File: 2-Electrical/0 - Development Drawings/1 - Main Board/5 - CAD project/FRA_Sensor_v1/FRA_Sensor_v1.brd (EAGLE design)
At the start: 100 x 100 mm, 179 parts, among them IC1 CP2101, IC2 LMV611, IC3 TS520533, IC4 ADS1115BQDGSRQ1, IC5 ADS1115BQDGSRQ1, IC6 ADS1115BQDGSRQ1, J2 ETH_CONN, J5 WM9734TR-ND, J8 1140084168, Q1 Si2300DS, Q2 FDN306P, Q3 Si2300DS, Q4 Si2300DS, Q5 Si2300DS, Q6 Si2300DS, Q7 100A/100V/6.8mΩ, T1 BC847, T2 BC847, T3 BC847, U2 ESP-WROOM-32, X1 TB001-500-02BE, Y3 32.768kHz

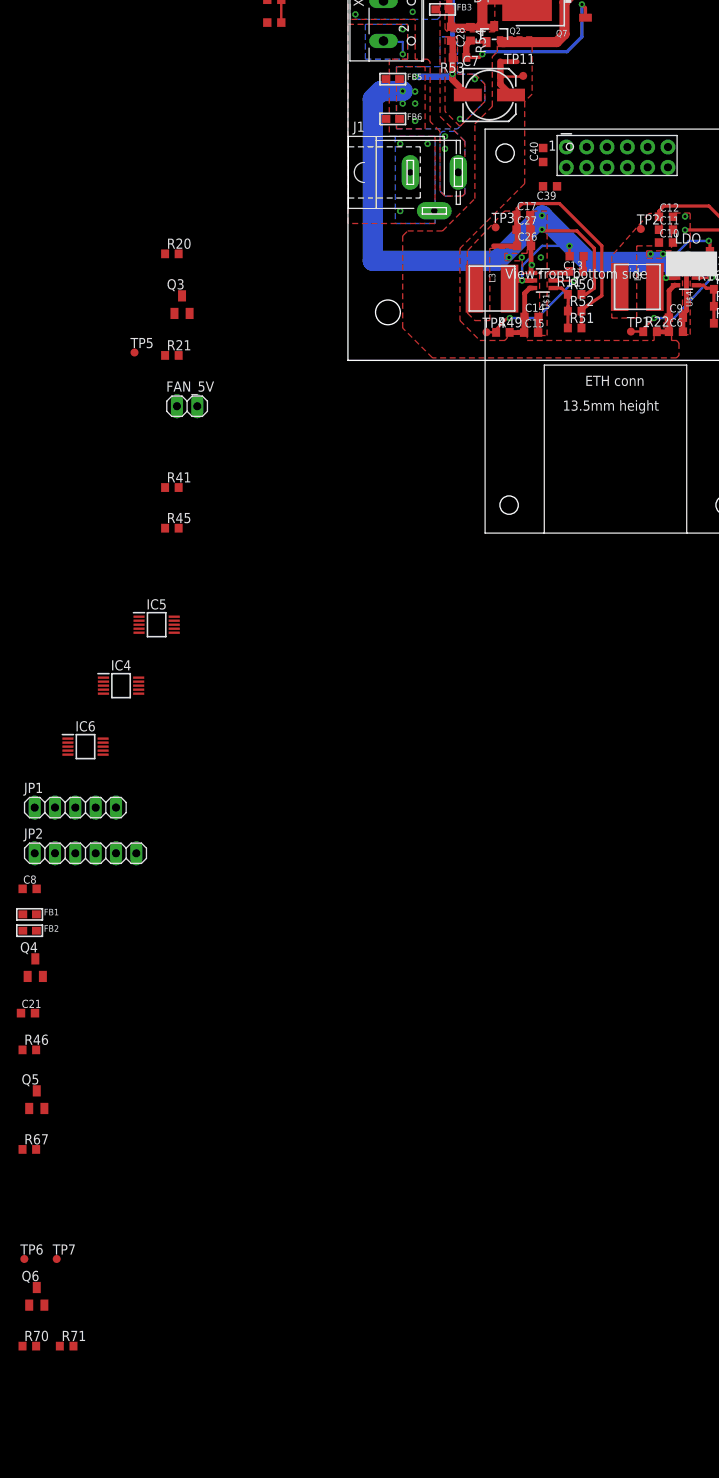
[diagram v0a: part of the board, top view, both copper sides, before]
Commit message: sch cap miltuplier add
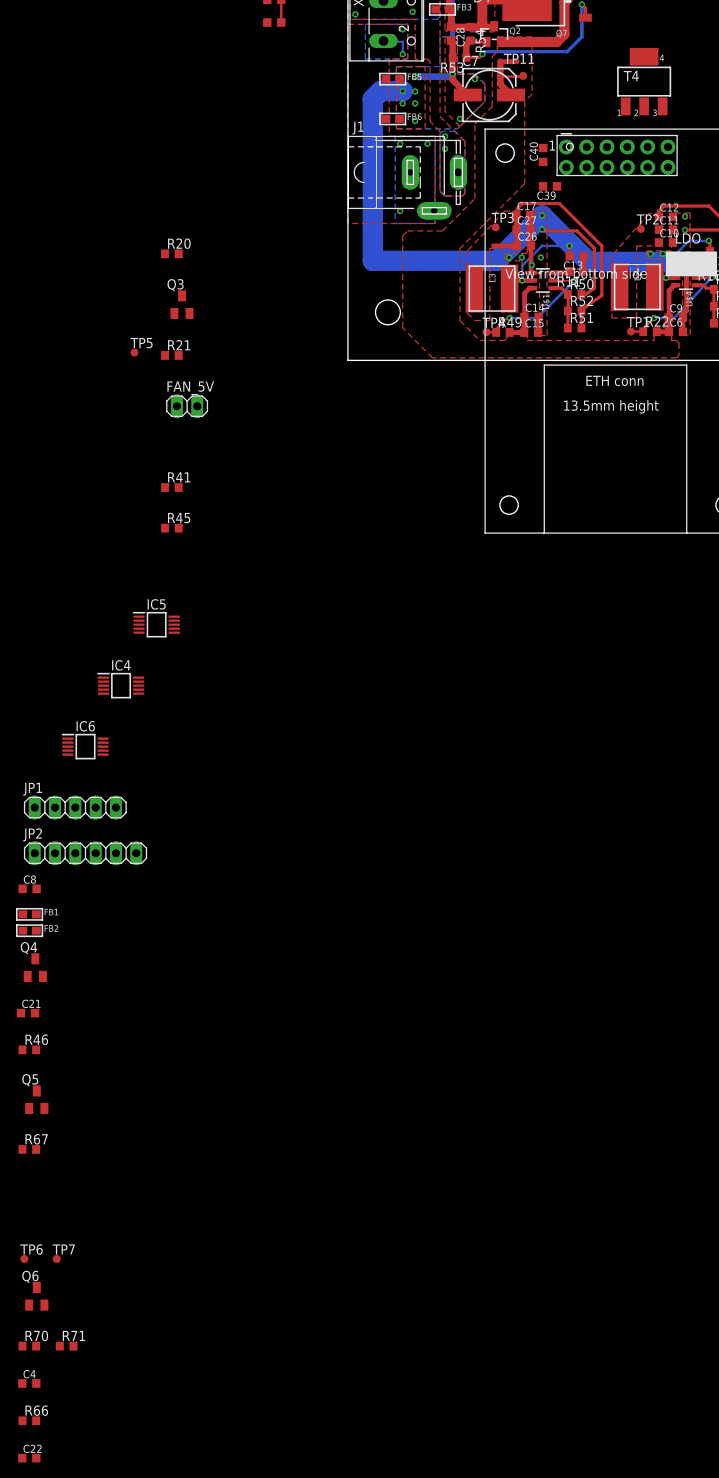
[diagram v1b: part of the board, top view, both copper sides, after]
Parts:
- added C22, C4: 10u, resistor:C0603K
- added R66: 10k, resistor:R0603
- added T4: (no value), transistor-neu-to92:SOT223
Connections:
- new net N$12: C22.1, C4.1, R66.2, T4.1
- new net VIN_FILT: T4.3
- net GND: now also C22.2, C4.2
- net VIN_PROTECTED: now also R66.1, T4.4
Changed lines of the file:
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@@
 <element name="FB6" library="microbuilder" package="0603" value="" x="5.6007" y="30.18155"/>
 <element name="Q7" library="microbuilder" package="TO252" value="100A/100V/6.8mΩ" x="24.892" y="45.11675" rot="R90"/>
+<element name="T4" library="transistor-neu-to92" package="SOT223" value="" x="37.02685" y="34.8488"/>
+<element name="C4" library="resistor" package="C0603K" value="10u" x="-39.8272" y="-127.88265"/>
+<element name="R66" library="resistor" package="R0603" value="10k" x="-39.8272" y="-132.5499"/>
+<element name="C22" library="resistor" package="C0603K" value="10u" x="-39.8272" y="-137.21715"/>
 </elements>
 <signals>
@@
 <wire x1="13.0683" y1="40.1206" x2="12.9032" y2="39.9555" width="0.6096" layer="16"/>
 <wire x1="14.99485" y1="49.02345" x2="16.89485" y2="49.02345" width="0.6096" layer="1"/>
-<wire x1="85.375" y1="56.06415" x2="87.9856" y2="65.99785" width="0" layer="19" extent="1-1"/>
-<wire x1="98.79" y1="41.34915" x2="96.76765" y2="49.1617" width="0" layer="19" extent="1-1"/>
-<wire x1="66.421" y1="17.907" x2="75.40625" y2="17.6276" width="0" layer="19" extent="1-1"/>
-<wire x1="65.408275" y1="12.8404125" x2="66.421" y2="17.907" width="0" layer="19" extent="1-1"/>
-<wire x1="58.801" y1="17.907" x2="66.421" y2="17.907" width="0" layer="19" extent="1-1"/>
-<wire x1="59.93" y1="22.86" x2="58.801" y2="17.907" width="0" layer="19" extent="1-1"/>
-<wire x1="50.927" y1="15.875" x2="58.801" y2="17.907" width="0" layer="19" extent="1-1"/>
-<wire x1="48.22825" y1="14.9352" x2="50.927" y2="15.875" width="0" layer="19" extent="1-1"/>
+<contactref element="C4" pad="2"/>
+<contactref element="C22" pad="2"/>
+<wire x1="-38.9522" y1="-127.88265" x2="-38.9522" y2="-137.21715" width="0" layer="19" extent="1-1"/>
+<wire x1="-39.116190625" y1="-81.593459375" x2="-38.9522" y2="-127.88265" width="0" layer="19" extent="1-1"/>
+<wire x1="-38.129790625" y1="-77.00579375" x2="-39.116190625" y2="-81.593459375" width="0" layer="19" extent="1-1"/>
+<wire x1="-38.9141" y1="-66.05905" x2="-38.129790625" y2="-77.00579375" width="0" layer="19" extent="1-1"/>
+<wire x1="-22.8591" y1="-20.97405" x2="-38.9141" y2="-66.05905" width="0" layer="19" extent="1-1"/>
+<wire x1="-21.1591" y1="0.61595" x2="-22.8591" y2="-20.97405" width="0" layer="19" extent="1-1"/>
+<wire x1="-19.7891" y1="5.86595" x2="-21.1591" y2="0.61595" width="0" layer="19" extent="1-1"/>
+<wire x1="3.1115" y1="12.446" x2="-19.7891" y2="5.86595" width="0" layer="19" extent="1-16"/>
+<wire x1="50.927" y1="15.875" x2="48.22825" y2="14.9352" width="0" layer="19" extent="1-1"/>
 <wire x1="24.3866375" y1="21.750084375" x2="24.2697" y2="18.10385" width="0" layer="19" extent="1-1"/>
 <wire x1="24.40305" y1="26.54805" x2="24.3866375" y2="21.750084375" width="0" layer="19" extent="1-1"/>
 <wire x1="27.305" y1="26.67" x2="24.40305" y2="26.54805" width="0" layer="19" extent="1-1"/>
 <wire x1="50.927" y1="1.905" x2="47.4463" y2="8.88365" width="0" layer="19" extent="1-1"/>
+<wire x1="58.801" y1="17.907" x2="50.927" y2="15.875" width="0" layer="19" extent="1-1"/>
+<wire x1="59.93" y1="22.86" x2="58.801" y2="17.907" width="0" layer="19" extent="1-1"/>
+<wire x1="66.421" y1="17.907" x2="58.801" y2="17.907" width="0" layer="19" extent="1-1"/>
+<wire x1="65.408275" y1="12.8404125" x2="66.421" y2="17.907" width="0" layer="19" extent="1-1"/>
 <wire x1="40.005" y1="26.67" x2="40.626" y2="17.9451" width="0" layer="19" extent="1-1"/>
+<wire x1="75.40625" y1="17.6276" x2="66.421" y2="17.907" width="0" layer="19" extent="1-1"/>
+<wire x1="96.76765" y1="49.1617" x2="98.79" y2="41.34915" width="0" layer="19" extent="1-1"/>
+<wire x1="87.9856" y1="65.99785" x2="85.375" y2="56.06415" width="0" layer="19" extent="1-1"/>
 <wire x1="13.97" y1="60.565" x2="13.2412" y2="49.02345" width="0" layer="19" extent="1-1"/>
 <wire x1="11.43" y1="60.96" x2="13.97" y2="60.565" width="0" layer="19" extent="1-1"/>
@@
 <wire x1="21.59" y1="60.96" x2="19.05" y2="60.565" width="0" layer="19" extent="1-1"/>
 <wire x1="-8.3325" y1="42.2275" x2="3.1115" y2="32.67075" width="0" layer="19" extent="1-16"/>
-<wire x1="-19.7891" y1="5.86595" x2="3.1115" y2="12.446" width="0" layer="19" extent="1-16"/>
-<wire x1="-21.1591" y1="0.61595" x2="-19.7891" y2="5.86595" width="0" layer="19" extent="1-1"/>
-<wire x1="-22.8591" y1="-20.97405" x2="-21.1591" y2="0.61595" width="0" layer="19" extent="1-1"/>
 <wire x1="-37.885" y1="50.8" x2="-8.3325" y2="45.085" width="0" layer="19" extent="1-1"/>
 <wire x1="-10.82675" y1="91.06535" x2="11.43" y2="60.96" width="0" layer="19" extent="1-1"/>
 <wire x1="-25.76195" y1="96.012" x2="-10.82675" y2="91.06535" width="0" layer="19" extent="1-1"/>
-<wire x1="-38.9141" y1="-66.05905" x2="-22.8591" y2="-20.97405" width="0" layer="19" extent="1-1"/>
-<wire x1="-38.129790625" y1="-77.00579375" x2="-38.9141" y2="-66.05905" width="0" layer="19" extent="1-1"/>
-<wire x1="-39.116190625" y1="-81.593459375" x2="-38.129790625" y2="-77.00579375" width="0" layer="19" extent="1-1"/>
 <wire x1="210.185" y1="67.07" x2="98.79" y2="59.34915" width="0" layer="19" extent="1-16"/>
 <wire x1="212.725" y1="65.62" x2="210.22" y2="67.07" width="0" layer="19" extent="16-16"/>
@@
 <wire x1="27.07005" y1="40.76065" x2="26.09545" y2="39.78605" width="1.27" layer="1"/>
 <wire x1="26.09545" y1="39.78605" x2="19.23165" y2="39.78605" width="1.27" layer="1"/>
+<contactref element="T4" pad="4"/>
+<contactref element="R66" pad="1"/>
+<wire x1="20.23655" y1="3.47345" x2="-40.6772" y2="-132.5499" width="0" layer="19" extent="1-1"/>
+<wire x1="37.02685" y1="37.9478" x2="27.07005" y2="40.76065" width="0" layer="19" extent="1-1"/>
 </signal>
 <signal name="SCLK">
@@
 <wire x1="4.5485" y1="39.8272" x2="6.8453" y2="39.8272" width="0.254" layer="16"/>
 </signal>
+<signal name="N$12">
+<contactref element="C4" pad="1"/>
+<contactref element="T4" pad="1"/>
+<contactref element="R66" pad="2"/>
+<contactref element="C22" pad="1"/>
+<wire x1="-38.9772" y1="-132.5499" x2="-40.7022" y2="-137.21715" width="0" layer="19" extent="1-1"/>
+<wire x1="-40.7022" y1="-127.88265" x2="-38.9772" y2="-132.5499" width="0" layer="19" extent="1-1"/>
+<wire x1="34.71545" y1="31.75" x2="-40.7022" y2="-127.88265" width="0" layer="19" extent="1-1"/>
+</signal>
+<signal name="VIN_FILT">
+<contactref element="T4" pad="3"/>
+</signal>
 </signals>

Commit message: datasheets, sch update
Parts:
- added IC7: LMP91000SD_NOPB, SamacSys_Parts:SON50P400X400X80-15N
- added IC8: PCA9555PW, micro-philips:TSSOP24
- added JP3, JP4, JP5, JP6, JP7, JP8, JP9: (no value), pinhead:2X03
- added U1: PCA9509DP, nxp_60:SOT505-1
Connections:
- new net ADCXX: JP3.1
- new net AGND: IC7.7
- new net AGND?: JP3.3
- new net DAP: IC7.15
- new net DGND: IC7.1
- new net MENB_DO: JP3.6
- new net VDD: IC7.6, IC8.24
- new net VSS: IC8.12
- net 3.3V: now also U1.1, U1.5
- net 5V: now also JP3.5, U1.8
- net GND: now also U1.4
- net SCL: now also JP3.4, U1.3
- net SCL_5V: now also U1.6
- net SDA: now also JP3.2, U1.2
- net SDA_5V: now also U1.7

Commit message: ldo addded
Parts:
- removed Q5, Q6: Si2300DS, adafruit:SOT23
- removed R67, R70, R71: 10k, resistor:R0603
- removed TP6, TP7: TPTP10R, testpad:TP10R
- added C37, C41: 1u, resistor:C0603K
- added C42, C43: 100n, resistor:C0603K
- added FID1, FID2, FID3, FID4: FIDUCIAL"", microbuilder:FIDUCIAL_1MM
- added IC9: LDK320ADU50R, SamacSys_Parts:ST-SOT-89
- C4: value 10u -> 1u
- R46: value 10k -> 0
- moved T4 186.9 mm to (222.5, 57.9), flipped to the bottom
- moved R46 128.2 mm to (-126.6, -180.5)
- moved IC8 1.68 mm to (-56.0, -144.7)
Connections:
- new net 5V_CALM: C41.1, IC9.2
- new net IN5VLDO: C37.1, IC9.3, R46.2
- net 3.3V: now also C43.1; no longer Q5.1, Q6.1, R46.1, R70.1
- net 5V: now also C42.1; no longer R67.1, R71.1
- net GND: now also C37.2, C41.2, C42.2, C43.2, IC9.1
- net SCL: no longer Q6.2, R70.2, TP7.TP
- net SCL_5V: no longer Q6.3, R71.2
- net SDA: no longer Q5.2, R46.2, TP6.TP
- net SDA_5V: no longer Q5.3, R67.2
- net VIN_PROTECTED: now also R46.1

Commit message: sch update
layout, od powerm SPIs,
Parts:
- removed JP1: (no value), pinhead:1X05
- removed JP2: (no value), pinhead:1X06
- removed JP3, JP4, JP5, JP6, JP7, JP8, JP9: (no value), pinhead:2X03
- removed LIGHT_DR1: LDR, pinhead:1X02
- removed SENSOR_1, SENSOR_2, SENSOR_3, SENSOR_4, SENSOR_5, SENSOR_6, SENSOR_7, SENSOR_8: SENS1, pinhead:1X04
- added Q10, Q11, Q5, Q6, Q8, Q9: FDN306P, microbuilder:SOT23-WIDE
- added R67, R70, R71, R72, R73, R74: 10k, resistor:R0603
- added U$10, U$11, U$12, U$3, U$8, U$9: CONN_03X2_WE_61200621621, FRA_eagle_lib:WE_61200621621
- moved R46 308.0 mm to (16.2, 92.4)
- moved C37 304.3 mm to (23.6, 95.5)
- moved C41 303.7 mm to (20.5, 93.3)
- moved IC9 302.7 mm to (19.0, 96.8)
- moved C42 277.2 mm to (51.7, 45.1)
- moved C43 267.1 mm to (51.7, 41.4), turned to 90 degrees
- moved U1 254.0 mm to (54.5, 43.2)
- moved IC8 230.9 mm to (45.7, 62.5)
- moved R23 152.8 mm to (79.6, 27.6)
- moved R55 146.7 mm to (86.8, 36.2), turned to 270 degrees
- moved R17 141.4 mm to (88.9, 36.2), turned to 270 degrees
- moved R63 136.9 mm to (84.8, 36.2), turned to 270 degrees
- moved R45 114.2 mm to (77.6, 34.8), turned to 180 degrees
- moved R41 113.6 mm to (78.5, 37.0)
- moved R32 73.2 mm to (72.1, 42.2), turned to 180 degrees
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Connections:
- removed net ADCXX: JP3.1
- removed net AGND?: JP3.3
- removed net MENB_DO: JP3.6
- removed net VIN_FILT: T4.3
- new net AA1: R66.1
- new net ADC1_1: U$3.2
- new net ADC1_2: U$8.2
- new net ADC1_3: U$9.2
- new net ADC1_4: U$10.2
- new net ADC2_1: U$11.2
- new net ADC2_2: U$12.2
- new net ENB_PWR_IF1: Q5.1, R67.2
- new net ENB_PWR_IF2: Q6.1, R70.2
- new net ENB_PWR_IF3: Q8.1, R71.2
- new net ENB_PWR_IF4: Q9.1, R72.2
- new net ENB_PWR_IF5: Q10.1, R73.2
- new net ENB_PWR_IF6: Q11.1, R74.2
- new net EN_IF1: Q5.3, R67.1, U$3.4
- new net EN_IF2: Q6.3, R70.1, U$8.4
- new net EN_IF3: Q8.3, R71.1, U$9.4
- new net EN_IF4: Q9.3, R72.1, U$10.4
- new net EN_IF5: Q10.3, R73.1, U$11.4
- new net EN_IF6: Q11.3, R74.1, U$12.4
- new net N$13: C22.2
- new net N$14: C4.2
- new net N$16: IC2.5
- new net N$18: R34.2
- new net N$27: C18.1
- new net V-: IC2.2
- net 5V: now also IC8.24, Q10.2, Q11.2, Q5.2, Q6.2, Q8.2, Q9.2; no longer IC2.5, JP3.5, R34.2
- net 5V_CALM: now also IC9.3, U$10.3, U$11.3, U$12.3, U$3.3, U$8.3, U$9.3; no longer IC9.2
- net AGND: now also U$10.1, U$11.1, U$12.1, U$3.1, U$8.1, U$9.1
- net GND: no longer C18.1, C22.2, C4.2, IC2.2, R35.1
- net IN5VLDO: now also IC9.2; no longer IC9.3
- net N$12: no longer T4.1
- net SCL: no longer JP3.4
- net SCL_5V: now also U$10.6, U$11.6, U$12.6, U$3.6, U$8.6, U$9.6
- net SDA: no longer JP3.2
- net SDA_5V: now also U$10.5, U$11.5, U$12.5, U$3.5, U$8.5, U$9.5
- net VDD: no longer IC8.24
- net VIN_PROTECTED: no longer R66.1, T4.4
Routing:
- net GND: track 334.4 -> 465.7 mm, vias 28 -> 39
- net MISO: track 0.00 -> 94.8 mm, vias 0 -> 5
- net MOSI: track 0.00 -> 94.2 mm, vias 0 -> 2
- net SCLK: track 0.00 -> 88.3 mm, vias 0 -> 4
- net ETH_CS: track 0.00 -> 84.6 mm, vias 0 -> 2
- net ETH_RST: track 0.00 -> 79.7 mm, vias 0 -> 2
- net 3.3V: track 73.8 -> 147.0 mm, vias 3 -> 8
- net ETH_INT: track 0.00 -> 54.1 mm, vias 0 -> 2
- net SD_CS: track 0.00 -> 53.1 mm
- net 5V: track 33.4 -> 60.8 mm, vias 0 -> 4
- net SCL_MCU: track 0.00 -> 26.9 mm, vias 0 -> 2
- net SDA_MCU: track 0.00 -> 23.1 mm, vias 0 -> 2
- net SD_CD: track 0.00 -> 23.0 mm
- net SD_VDD: track 0.00 -> 12.5 mm
- net GPIO0: track 31.5 -> 35.2 mm, vias 3 -> 4
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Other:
- board text added: "1"
- board text added: "15"
- board text added: "25"
- board text added: "38"

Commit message: sch update
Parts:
- removed D7: (no value), SparkFun-LED:LED_5MM
- removed IC6: ADS1115BQDGSRQ1, SamacSys_Parts:SOP50P490X110-10N
- removed Q4: Si2300DS, adafruit:SOT23
- removed R14, R15, R18: 100, resistor:R0603
- removed R41: 0(DNI), resistor:R0603
- removed R45: 0, resistor:R0603
- removed R69: 10K, resistor:R0603
- removed S2: (no value), adafruit:B3F-31XX
- removed U$5, U$6: MOUNTINGHOLE3.0THIN, microbuilder:MOUNTINGHOLE_3.0_PLATEDTHIN
- added C44, C45, C46, C47, C48, C49, C50, C51, C52: 100n, resistor:C0603K
- added FB7, FB8, FB9: (no value), microbuilder:0603
- added Q12, Q13, Q14, Q15, Q16, Q17: FDN306P, microbuilder:SOT23-WIDE
- added R75, R76, R77, R78, R79, R80, R81, R82, R83, R84, R85, R86, R87, R88, R89, R90: 10k, resistor:R0603
- added TP10, TP12, TP13, TP14, TP15, TP16, TP17, TP18, TP19, TP20, TP6, TP7, TP8, TP9: TPTP10R, testpad:TP10R
- added U$13, U$14, U$15, U$16, U$17, U$18: CONN_03X2_WE_61200621621, FRA_eagle_lib:WE_61200621621
- C21: value 10u -> 100n
- moved IC7 308.9 mm to (218.4, 25.5), flipped to the bottom
- moved C22 299.4 mm to (212.8, 23.3), flipped to the bottom
- moved C4 299.4 mm to (212.8, 32.7), flipped to the bottom
- moved R66 299.4 mm to (212.8, 28.0), flipped to the bottom
- moved C21 198.3 mm to (24.0, 106.1), turned to 90 degrees
- moved FB2 150.6 mm to (44.1, 53.8), turned to 270 degrees
- moved R19 146.2 mm to (78.5, 28.2)
- moved FB1 143.5 mm to (35.0, 53.2), turned to 270 degrees
- moved IC5 138.0 mm to (70.7, 67.5)
- moved C8 130.3 mm to (38.0, 38.5)
- moved S1 124.9 mm to (95.9, 71.7)
- moved R9 123.6 mm to (84.5, 61.1)
- moved IC4 117.4 mm to (19.2, 66.7)
- moved C24 107.6 mm to (96.9, 60.5), turned to 90 degrees
- moved C25 105.6 mm to (95.2, 60.5), turned to 90 degrees
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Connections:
- removed net N$10: Q4.3
- removed net N$7: D7.A, R14.1, R15.1
- removed net N$9: D7.K, R41.1, R45.2
- removed net VSS: IC8.12
- new net +5V/1: C44.1, C45.1, FB1.2, FB9.2, IC4.1, IC4.8, IC5.8, IC8.24, Q10.2, Q11.2, Q12.2, Q13.2, Q14.2, Q15.2, Q16.2, Q17.2, Q5.2, Q6.2, Q8.2, Q9.2, R81.1, R82.1, U1.8
- new net 1AIN0: C21.1, IC5.4, R83.1
- new net 1AIN1: C46.1, IC5.5, R84.1
- new net 1AIN2: C47.1, IC5.7, R85.1
- new net 1AIN3: C48.1, IC5.6, R86.1
- new net 2AIN0: C49.1, IC4.4, R87.1
- new net 2AIN1: C50.1, IC4.5, R88.1
- new net 2AIN2: C51.1, IC4.7, R89.1
- new net 2AIN3: C52.1, IC4.6, R90.1
- new net 5V_CALM_LDO: C41.1, FB7.1, IC9.3
- new net ADC2_3: R89.2, U$13.2
- new net ADC2_4: R90.2, U$14.2
- new net ADC3_1: U$15.2
- new net ADC3_2: U$16.2
- new net ADC3_3: U$17.2
- new net ADC3_4: U$18.2
- new net ENB_PWR_IF10: Q15.1, R78.2
- new net ENB_PWR_IF11: Q16.1, R79.2
- new net ENB_PWR_IF12: Q17.1, R80.2
- new net ENB_PWR_IF7: IC8.10, Q12.1, R75.2
- new net ENB_PWR_IF8: IC8.11, Q13.1, R76.2
- new net ENB_PWR_IF9: Q14.1, R77.2
- new net EN_IF10: Q15.3, R78.1, U$16.4
- new net EN_IF11: Q16.3, R79.1, U$17.4
- new net EN_IF12: Q17.3, R80.1, U$18.4
- new net EN_IF7: Q12.3, R75.1, U$13.4
- new net EN_IF8: Q13.3, R76.1, U$14.4
- new net EN_IF9: Q14.3, R77.1, U$15.4
- new net N$29: TP6.TP, U2.5
- new net N$30: TP7.TP, U2.4
- new net N$31: TP8.TP, U2.11
- new net N$33: TP9.TP, U2.12
- new net N$37: IC4.2, TP12.TP
- new net N$40: IC5.2, TP10.TP
- new net N$41: IC8.1, TP13.TP
- new net N$42: IC8.13, TP14.TP
- new net N$43: IC8.14, TP15.TP
- new net N$44: IC8.15, TP16.TP
- new net N$45: IC8.16, TP17.TP
- new net N$46: IC8.17, TP18.TP
- net 3.3V: no longer R14.2, R15.2, R18.2, R69.2
- net 5V: now also FB1.1, FB9.1; no longer IC8.24, Q10.2, Q11.2, Q5.2, Q6.2, Q8.2, Q9.2, U1.8
- net 5V_CALM: now also FB7.2, U$13.3, U$14.3, U$15.3, U$16.3, U$17.3, U$18.3; no longer C41.1, IC9.3
- net ADC1_1: now also R83.2
- net ADC1_2: now also R84.2
- net ADC1_3: now also R85.2
- net ADC1_4: now also R86.2
- net ADC2_1: now also R87.2
- net ADC2_2: now also R88.2
- net AGND: now also C21.2, C44.2, C45.2, C46.2, C47.2, C48.2, C49.2, C50.2, C51.2, C52.2, FB2.2, FB8.2, IC4.3, IC5.1, IC5.3, IC8.12, IC8.2, IC8.21, IC8.3, U$13.1, U$14.1, U$15.1, U$16.1, U$17.1, U$18.1
- net BTN1: now also U2.6
- net BTN2: now also U2.7; no longer R69.1, S2.1
- net ENB_PWR_IF1: now also IC8.4
- net ENB_PWR_IF2: now also IC8.5
- net ENB_PWR_IF3: now also IC8.6
- net ENB_PWR_IF4: now also IC8.7
- net ENB_PWR_IF5: now also IC8.8
- net ENB_PWR_IF6: now also IC8.9
- net GND: now also FB2.1, FB8.1, TP20.TP; no longer C21.2, Q4.2, R45.1, S2.2
- net GPIO0: no longer R41.2
- net N$6: no longer R18.1
- net NRST: now also TP19.TP
- net SCL_5V: now also IC4.10, IC5.10, IC8.22, R82.2, U$13.6, U$14.6, U$15.6, U$16.6, U$17.6, U$18.6
- net SDA_5V: now also IC4.9, IC5.9, IC8.23, R81.2, U$13.5, U$14.5, U$15.5, U$16.5, U$17.5, U$18.5
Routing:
- net GND: track 465.7 -> 597.8 mm, vias 39 -> 53
- net 3.3V: track 147.0 -> 258.8 mm, vias 8 -> 15
- net SDA: track 0.00 -> 31.6 mm
- net SCL: track 0.00 -> 28.3 mm
- net BTN1: track 0.00 -> 17.5 mm
- net N$30: track 0.00 -> 16.3 mm, vias 0 -> 2
- net VIN_PROTECTED: track 41.0 -> 55.5 mm
- net LED: track 0.00 -> 13.7 mm, vias 0 -> 1
- net IN5VLDO: track 0.00 -> 11.5 mm, vias 0 -> 6
- net N$6: track 0.00 -> 8.76 mm, vias 0 -> 1
- net N$5: track 0.00 -> 6.81 mm
- net N$4: track 0.00 -> 6.16 mm
- net 5V_CALM_LDO: track 0.00 -> 5.97 mm
- net N$29: track 0.00 -> 5.73 mm, vias 0 -> 2
- net MTDI: track 4.27 -> 8.84 mm
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- added copper zone on layer 1, net IN5VLDO
- added copper zone on layer 16, net IN5VLDO
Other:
- board text added: "14"
- board text added: "5V_calm"
- board text removed: "15"
